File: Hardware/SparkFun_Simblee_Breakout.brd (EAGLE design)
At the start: 25.4 x 48.3 mm, 18 parts, among them U1 ADP160, U2 RFD77101

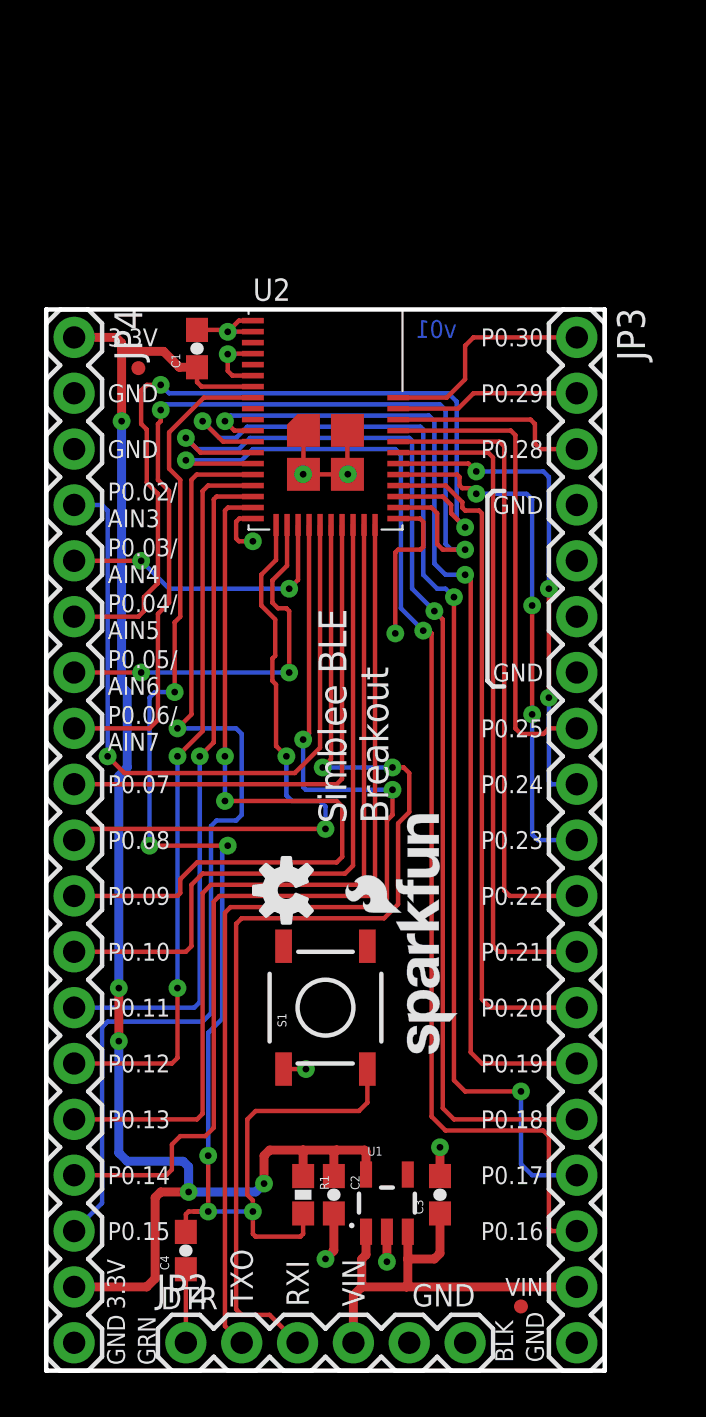
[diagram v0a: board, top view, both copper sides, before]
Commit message: Major changes to make compatible with RFDigital stuff
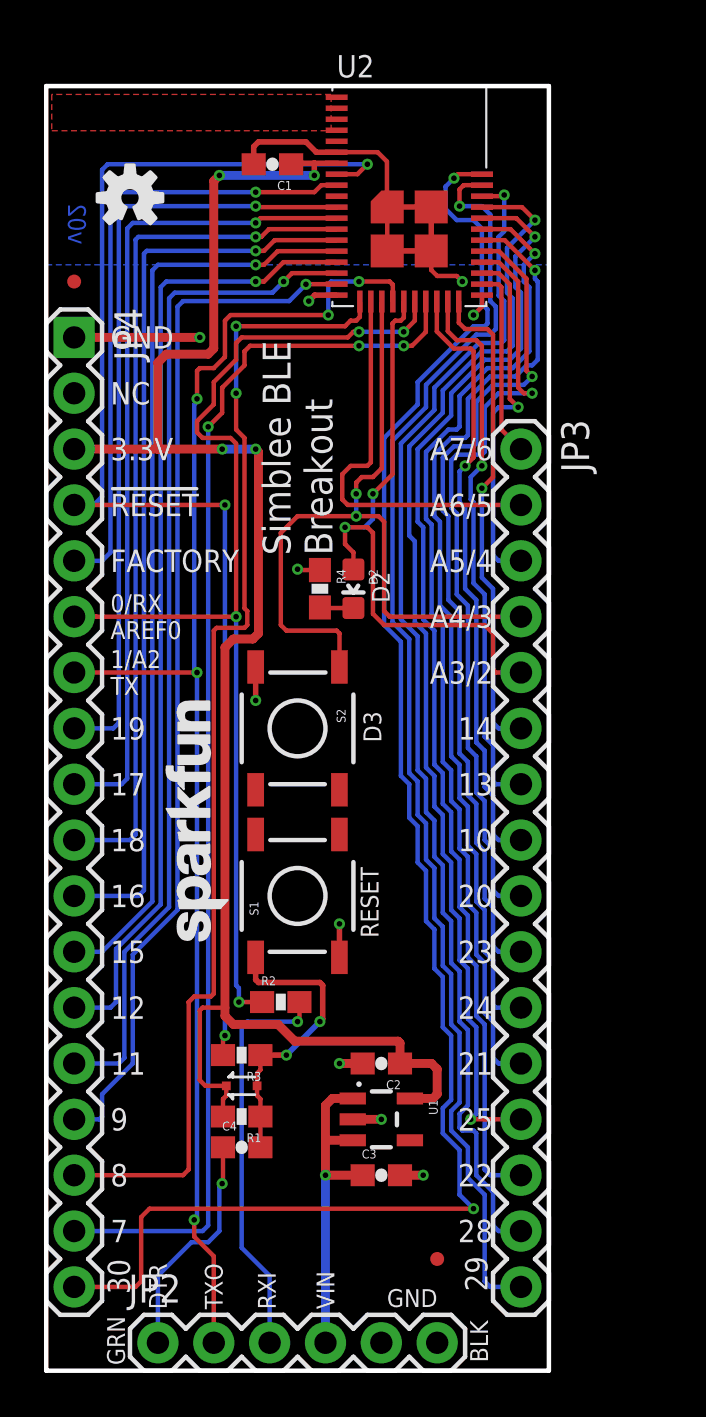
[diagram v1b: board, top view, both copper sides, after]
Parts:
- added D1: RB751, SparkFun-DiscreteSemi:SOD-523
- added D2: RED, SparkFun-LED:LED-0603
- added R2, R4: 1K, SparkFun-Resistors:0603-RES
- added R3: 100, SparkFun-Resistors:0603-RES
- added S2: SWITCH-MOMENTARY-2SMD, SparkFun-Electromechanical:TACTILE-SWITCH-SMD
- JP3: device SparkFun-Connectors:1X19 -> SparkFun-Connectors:1X16
- JP4: device SparkFun-Connectors:1X19 -> SparkFun-Connectors:1X18
- LOGO1, LOGO3: value SFE_LOGO_NAME_FLAME.1_INCH -> SFE_LOGO_NAME.1_INCH; device SparkFun-Aesthetics:SFE_LOGO_NAME_FLAME_.1 -> SparkFun-Aesthetics:SFE_LOGO_NAME_.1
- moved LOGO4 43.5 mm to (3.81, 53.3)
- moved LOGO2 32.3 mm to (3.81, 53.3), turned to 0 degrees
- moved LOGO3 15.7 mm to (17.7, 29.7), turned to 270 degrees
- moved LOGO1 11.2 mm to (8.76, 19.1)
- moved U2 10.9 mm to (13.2, 57.9)
- moved C1 9.06 mm to (10.3, 54.9), turned to 180 degrees
- moved C2 6.35 mm to (15.2, 14.0), turned to 180 degrees
- moved JP3 5.68 mm to (21.6, 41.9)
- moved C4 5.34 mm to (8.89, 10.2), turned to 0 degrees
- moved S1 5.24 mm to (11.4, 21.6)
- moved FID2 4.90 mm to (1.27, 49.5)
- moved R1 4.52 mm to (8.89, 11.6), turned to 180 degrees
- moved FID1 4.38 mm to (17.8, 5.08)
- moved U1 3.82 mm to (15.2, 11.4), turned to 270 degrees
- moved C3 2.81 mm to (15.2, 8.89), turned to 0 degrees
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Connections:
- new net !RESET: JP4.4, R3.2, U2.8
- new net FACTORY: JP4.5, U2.9
- new net N$2: D2.C, R4.2
- new net RXI_PROTECTED: JP4.6, R2.1, U2.25
- new net SI_STRIP: U2.1, U2.2, U2.4
- net 3.3V: now also D1.C, JP4.3, R1.2; no longer JP4.1, JP4.18, R1.1
- net GND: now also JP4.1, R4.1, S1.3, S2.3; no longer JP3.19, JP3.4, JP3.5, JP3.6, JP3.7, JP4.19, JP4.2, JP4.3, S1.1, U2.1, U2.2, U2.4
- net N$1: now also D1.A, R1.1, R3.1, S1.1; no longer R1.2, S1.3, U2.8
- net P0.02/AIN3: now also D2.A, JP3.5; no longer JP4.4
- net P0.03/AIN4: now also JP3.4, S2.1; no longer JP4.5
- net P0.04/AIN5: now also JP3.3; no longer JP4.6
- net P0.05/AIN6: now also JP3.2; no longer JP4.7
- net P0.06/AIN7: now also JP3.1; no longer JP4.8
- net P0.07: now also JP4.17; no longer JP4.9
- net P0.08: now also JP4.16; no longer JP4.10
- net P0.09: now also JP4.15; no longer JP4.11
- net P0.10: now also JP3.8; no longer JP4.12
- net P0.11: now also JP4.14; no longer JP4.13
- net P0.12: now also JP4.13; no longer JP4.14
- net P0.13: now also JP3.7; no longer JP4.15
- net P0.14: now also JP3.6; no longer JP4.16
- net P0.15: now also JP4.12; no longer JP4.17
- net P0.16: now also JP4.11; no longer JP3.17
- net P0.17: now also JP4.9; no longer JP3.16
- net P0.18: now also JP4.10; no longer JP3.15
- net P0.19: now also JP4.8; no longer JP3.14
- net P0.20: now also JP3.9; no longer JP3.13
- net P0.22: now also JP3.14; no longer JP3.11
- net P0.24: now also JP3.11; no longer JP3.9
- net P0.25: now also JP3.13; no longer JP3.8
- net P0.28: now also JP3.15; no longer JP3.3
- net P0.29: now also JP3.16; no longer JP3.2
- net P0.30: now also JP4.18; no longer JP3.1
- net RXI: now also R2.2; no longer U2.25
- net TXO: now also JP4.7
- net VIN: no longer JP3.18
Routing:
- net P0.30: track 10.1 -> 75.2 mm, vias 0 -> 2
- net !RESET: track 0.00 -> 62.0 mm, vias 0 -> 3
- net N$1: track 65.7 -> 13.5 mm, vias 6 -> 2
- net RXI_PROTECTED: track 0.00 -> 51.1 mm, vias 0 -> 4
- net P0.29: track 8.41 -> 58.2 mm, vias 0 -> 1
- net P0.28: track 9.20 -> 54.4 mm, vias 0 -> 1
- net P0.06/AIN7: track 43.4 -> 8.67 mm, vias 2 -> 0
- net P0.07: track 23.8 -> 56.6 mm, vias 0 -> 3
- net RXI: track 50.1 -> 18.4 mm, vias 2 -> 1
- net P0.25: track 21.8 -> 50.4 mm, vias 0 -> 2
- net FACTORY: track 0.00 -> 28.5 mm, vias 0 -> 1
- net P0.08: track 27.8 -> 52.7 mm
- net P0.22: track 28.5 -> 51.3 mm, vias 0 -> 1
- net P0.04/AIN5: track 38.4 -> 16.3 mm, vias 2 -> 1
- net P0.03/AIN4: track 13.4 -> 34.7 mm
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- added copper zone on layer 1, net SI_STRIP
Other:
- board size 25.4 x 48.3 mm -> 22.9 x 58.4 mm
- board text added: "!RESET"
- board text added: "0/AREF0/RX"
- board text added: "0/RX AREF0"
- board text added: "1/A2 TX"
- board text added: "1/A2/TX"
- board text added: "10"
- board text added: "11"
- board text added: "12"
- board text added: "13"
- board text added: "14"
- board text added: "15"
- board text added: "16"
- board text added: "17"
- board text added: "18"
- board text added: "19"
- board text added: "20"
- board text added: "21"
- board text added: "22"
- board text added: "23"
- board text added: "24"
- board text added: "25"
- board text added: "28"
- board text added: "29"
- board text added: "30"
- board text added: "7"
- board text added: "8"
- board text added: "9"
- board text added: "A3/2"
- board text added: "A4/3"
- board text added: "A5/4"
- board text added: "A6/5"
- board text added: "A7/6"
- board text added: "D2"
- board text added: "D3"
- board text added: "Dimensions in inches"
- board text added: "FACTORY"
- board text added: "NC"
- board text added: "RESET"
- board text added: "v02"
- board text removed: "P0.02/ AIN3"
- board text removed: "P0.03/ AIN4"
- board text removed: "P0.04/ AIN5"
- board text removed: "P0.05/ AIN6"
- board text removed: "P0.06/ AIN7"
- board text removed: "P0.07"
- board text removed: "P0.08"
- board text removed: "P0.09"
- board text removed: "P0.10"
- board text removed: "P0.11"
- board text removed: "P0.12"
- board text removed: "P0.13"
- board text removed: "P0.14"
- board text removed: "P0.15"
- board text removed: "P0.16"
- board text removed: "P0.17"
- board text removed: "P0.18"
- board text removed: "P0.19"
- board text removed: "P0.20"
- board text removed: "P0.21"
- board text removed: "P0.22"
- board text removed: "P0.23"
- board text removed: "P0.24"
- board text removed: "P0.25"
- board text removed: "P0.28"
- board text removed: "P0.29"
- board text removed: "P0.30"
- board text removed: "v01"
